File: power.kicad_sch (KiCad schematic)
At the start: 29 parts, among them U21 TPS62A06DRLR, U22 INA228AQDGSRQ1, U23 INA187A2IDBVR

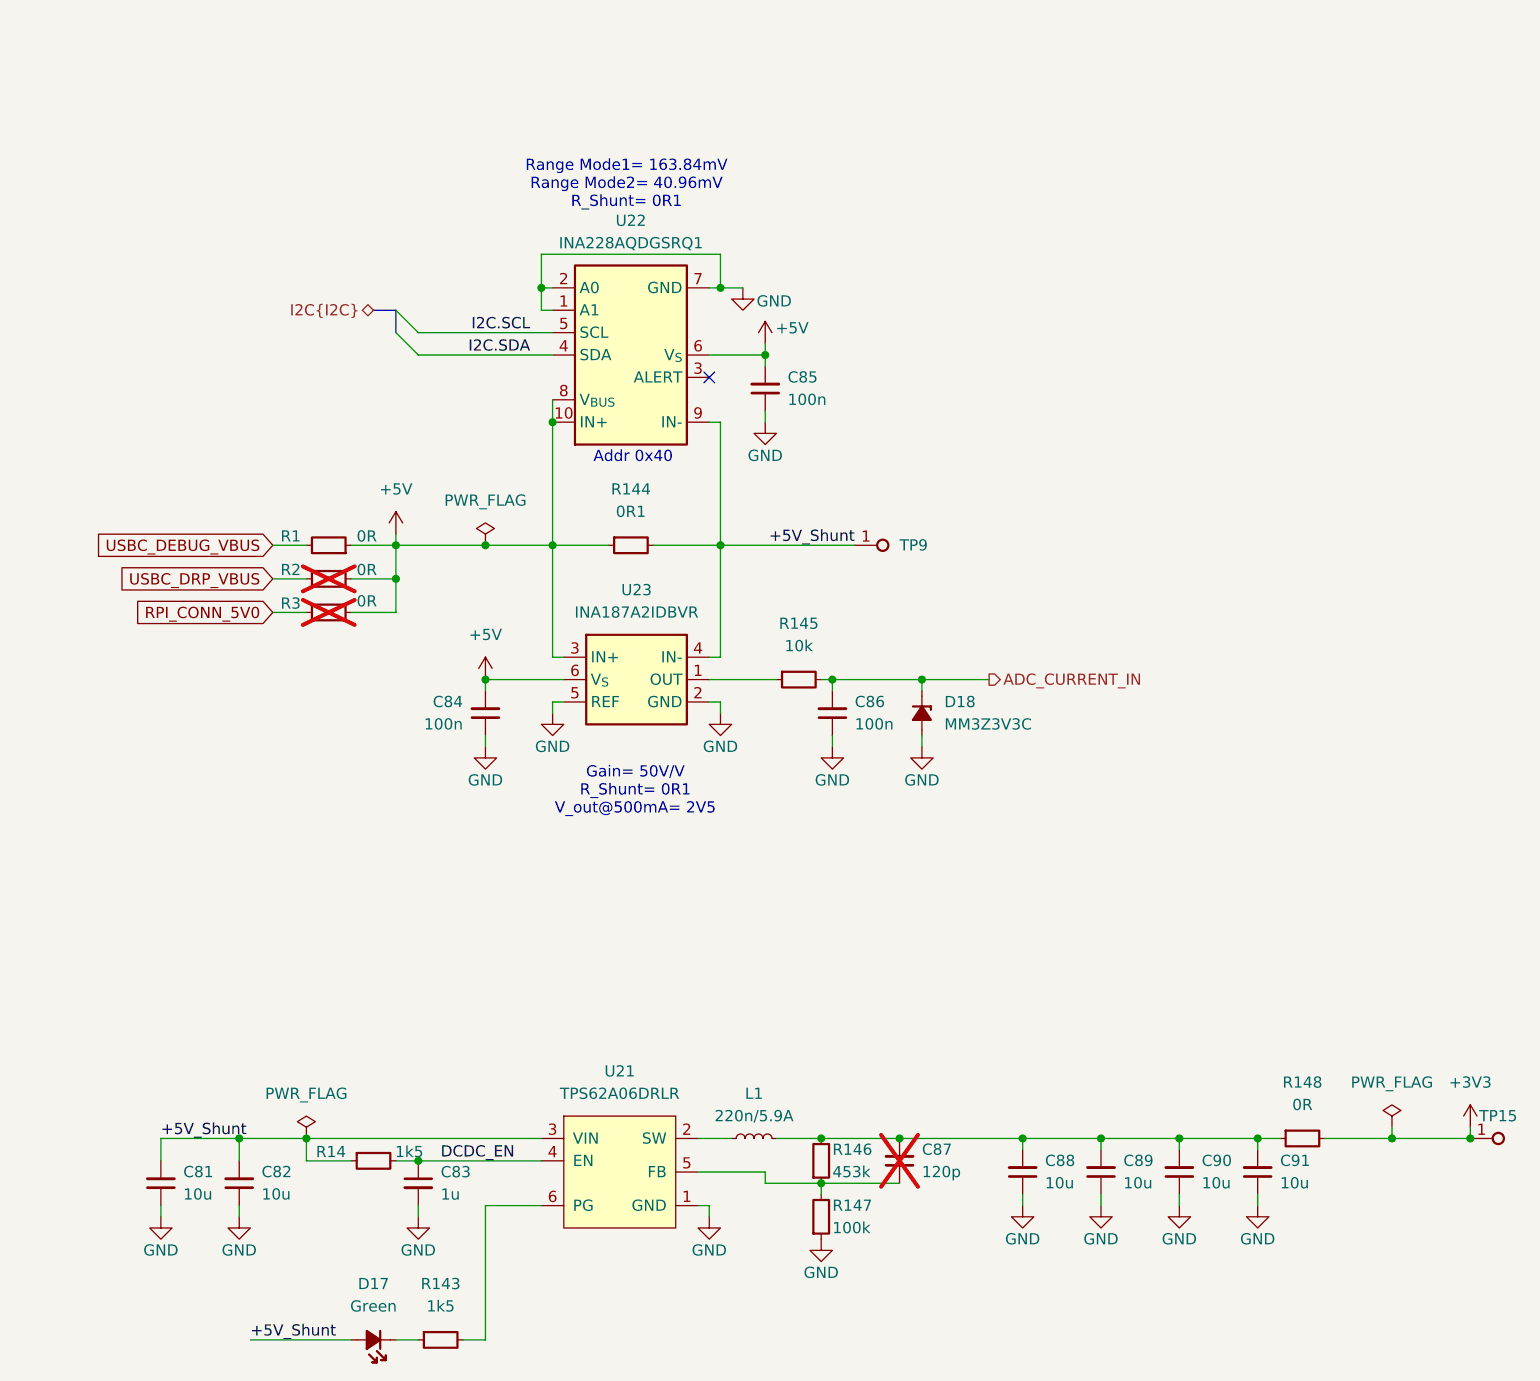
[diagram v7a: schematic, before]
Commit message: [#95036] Add schematic markings
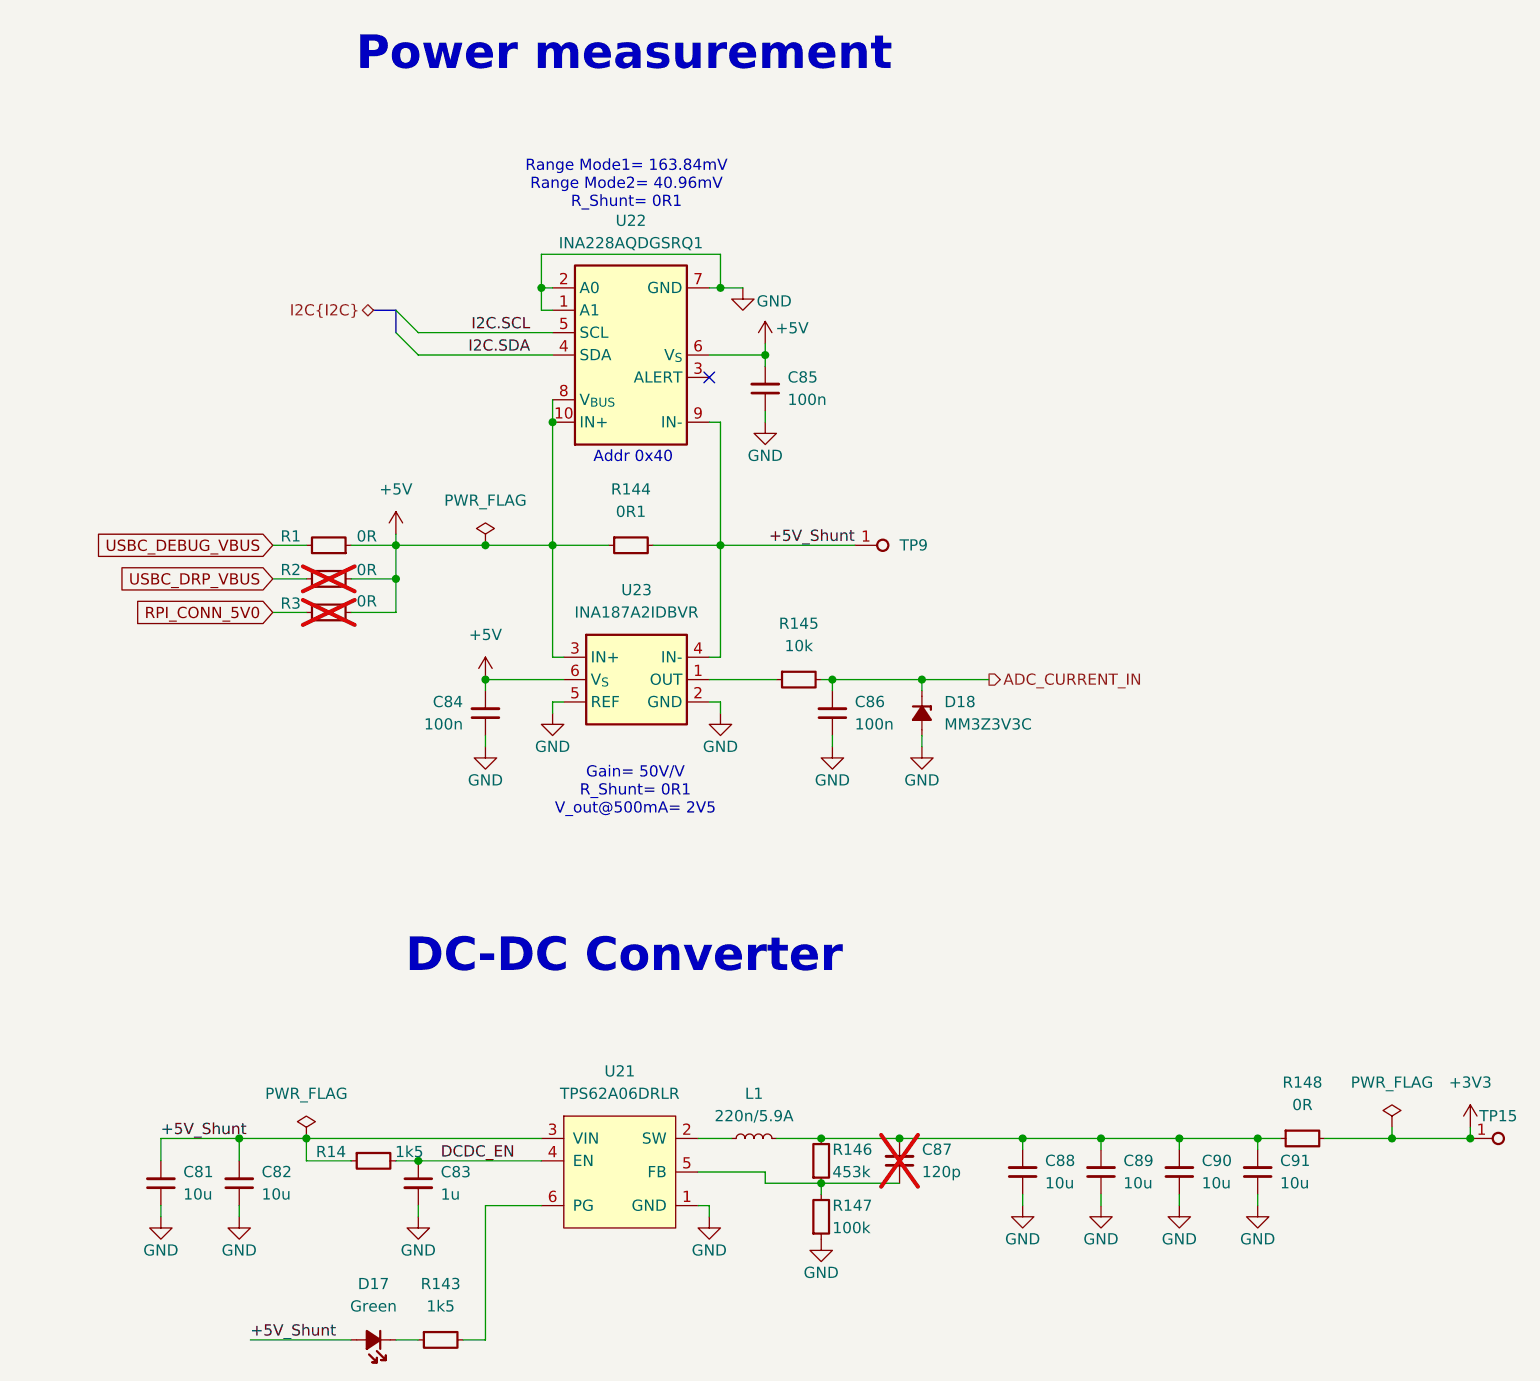
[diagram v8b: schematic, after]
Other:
- note added: "DC-DC Converter"
- note added: "Power measurement"
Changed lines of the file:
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@@
 		(company "Antmicro")
+	)
+	(text "Power measurement"
+		(exclude_from_sim no)
+		(at 182.118 52.578 0)
+		(effects
+			(font
+				(size 3.81 3.81)
+				(thickness 0.762)
+				(bold yes)
+			)
+			(justify top)
+		)
 	)
 	(text "Gain= 50V/V\nR_Shunt= 0R1\nV_out@500mA= 2V5 "
@@
 		)
 	)
+	(text "DC-DC Converter"
+		(exclude_from_sim no)
+		(at 182.118 154.94 0)
+		(effects
+			(font
+				(size 3.81 3.81)
+				(thickness 0.762)
+				(bold yes)
+			)
+			(justify top)
+		)
+	)
